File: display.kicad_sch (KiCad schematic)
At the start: 0 parts

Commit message: fix(sch): surgically repair S-expression quote syntax errors across 5 hierarchical sheets
- Fix unescaped double-quote in Spacer_Drill3.7mm_H4mm description on interfaces.kicad_sch line 1459
- Remove backslash-escaped quotes in symbol definitions and lib_id references across display, id-serial, som, and usb-debug sheets (332 lines)
- Restore clean hierarchical schematic loading in KiCad 10 GUI and CLI
- Verified with kicad-cli sch export netlist (full 300 components / 437 nets recovered) and sch erc
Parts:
- added C1, C2, C3, C4: C_4u7_0402, jetson-footprints:C_0402_1005Metric, symbol jetson-symbols:C_4u7_0402
- added C12, C26, C27, C39, C40, C42, C43, C44, C45, C5, C6, C7, C73, C74, C75, C76, C77, C78, C79, C8, C80: C_100n_0402, jetson-footprints:C_0402_1005Metric, symbol jetson-symbols:C_100n_0402
- added D10, D11, D12: PESD2USB5UV-TR, jetson-footprints:SOT-23-3, symbol jetson-symbols:PESD2USB5UV-TR
- added D2, D4: 1N4148WS, jetson-footprints:D_SOD-323F, symbol jetson-symbols:1N4148WS
- added IC11: SN74LV1T125DBVR, jetson-footprints:SOT-23-5, symbol jetson-symbols:SN74LV1T125DBVR
- added IC18, IC2: TPD8S009DSMR, jetson-footprints:R-PDSO-N15, symbol jetson-symbols:TPD8S009DSMR
- added IC6: PCA9517ADP, jetson-footprints:TSSOP-8_3x3mm_P0.65mm, symbol jetson-symbols:PCA9517ADP
- added J1: HDMI-Micro-D_Molex_467561001, jetson-footprints:HDMI-Micro-D_Receptacle_Molex_467651001, symbol jetson-symbols:HDMI-Micro-D_Molex_467561001
- added J15: Bus_DDR4_SODIMM_CUSTOM_Jetson-Nano-H9.2mm-socket, jetson-footprints:TE_2309413, symbol jetson-symbols:Bus_DDR4_SODIMM_CUSTOM_Jetson-Nano-H9.2mm-socket
- added J2: DisplayPort-Mini_TE_2129320-3, jetson-footprints:DisplayPort-Mini_Receptacle_TE_2129320-3, symbol jetson-symbols:DisplayPort-Mini_TE_2129320-3
- added L10, L8, L9: FB_120Z_3A_Murata-BLM18SG_0603, jetson-footprints:FB_0603_1608Metric, symbol jetson-symbols:FB_120Z_3A_Murata-BLM18SG_0603
- added R1, R10, R2, R3, R4, R7, R8, R9: R_5R6_0402, jetson-footprints:R_0402_1005Metric, symbol jetson-symbols:R_5R6_0402
- added R100, R26, R30: R_100k_0402, jetson-footprints:R_0402_1005Metric, symbol jetson-symbols:R_100k_0402
- added R11, R37, R5, R6, R81, R83, R88: R_2k_0402, jetson-footprints:R_0402_1005Metric, symbol jetson-symbols:R_2k_0402
- added R12, R82, R98, R99: R_0R_0402, jetson-footprints:R_0402_1005Metric, symbol jetson-symbols:R_0R_0402
- added R31, R32: R_1M_0402, jetson-footprints:R_0402_1005Metric, symbol jetson-symbols:R_1M_0402
- added T1: BSS138PW, jetson-footprints:SC70-3, symbol jetson-symbols:BSS138PW
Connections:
- new net: IC6.2 (SCLA), R81.2, R98.2
- new net: IC6.3 (SDAA), R11.2, R99.2
- new net: C3.1, C4.1, D2.1 (C), J2.20 (DP_PWR)
- new net: C1.1, C2.1, D4.1 (C), J1.19 (+5V)
- new net: R82.1, R83.1, T1.1 (G)
- new net: J1.16 (GND), R12.1
- new net 1V8_SYS: C5.1, IC11.5 (VCC), R88.1
- new net 3V3_SYS: C26.1, IC6.1 (V_{CC(A)}), L10.1, R11.1, R81.1
- new net 5V0_SYS: IC2.13 (VCC), IC2.15 (VCC), L9.1
- new net DP_CEC: J2.6 (CFG2), R32.1
- new net DP_HPD: IC11.4 (Y), J15.88 (DP0_HPD)
- new net DP_HPD_IN: D12.2, IC11.2 (A), J2.2 (HPD), R100.1
- new net DP_MODE: J2.4 (CFG1), R31.1
- new net DP_PWR: D2.2 (A), L10.2, R26.2
- new net EDP0_TX_N: C40.1, J15.39 (DP0_TXD0_N)
- new net EDP0_TX_P: C39.1, J15.41 (DP0_TXD0_P)
- new net EDP1_TX_N: C43.1, J15.45 (DP0_TXD1_N)
- new net EDP1_TX_P: C42.1, J15.47 (DP0_TXD1_P)
- new net EDP2_TX_N: C7.1, J15.51 (DP0_TXD2_N)
- new net EDP2_TX_P: C6.1, J15.53 (DP0_TXD2_P)
- new net EDP3_TX_N: C12.1, J15.57 (DP0_TXD3_N)
- new net EDP3_TX_P: C8.1, J15.59 (DP0_TXD3_P)
- new net EDP_AUX_N: C45.1, J15.90 (DP0_AUX_N)
- new net EDP_AUX_P: C44.1, J15.92 (DP0_AUX_P)
- new net EDP_C_AUX_C_N: C45.2, J2.18 (AUX-), R26.1
- new net EDP_C_AUX_C_P: C44.2, J2.16 (AUX+), R30.1
- new net GND: C1.2, C2.2, C26.2, C27.2, C3.2, C4.2, C5.2, D10.3, D11.3, D12.3, IC11.1 (~{OE}), IC11.3 (GND), IC18.11 (GND), IC18.2 (GND), IC18.5 (GND), IC18.8 (GND), IC2.11 (GND), IC2.2 (GND), IC2.5 (GND), IC2.8 (GND), IC6.4 (GND), J2.1 (GND), J2.13 (GND), J2.14 (GND), J2.19 (GND), J2.7 (GND), J2.8 (GND), J2.SH, L8.1, R100.2, R12.2, R30.2, R31.2, R32.2, R37.2, R83.2, T1.2 (S)
- new net HDMI_PWR: C27.1, D4.2 (A), IC18.13 (VCC), IC18.15 (VCC), IC6.5 (EN), IC6.8 (V_{CC(B)}), L9.2, R5.1, R6.1
- new net HDMI_SHIELD: J1.10 (D0S), J1.13 (CKS), J1.4 (D2S), J1.7 (D1S), J1.SH, L8.2
- new net M2_ALERT: J15.212 (GPIO10)
- new net ML_C_LANE0_N: C40.2, IC2.3 (D0-), J2.5 (TXD0-)
- new net ML_C_LANE0_P: C39.2, IC2.1 (D0+), J2.3 (TXD0+)
- new net ML_C_LANE1_N: C43.2, IC2.6 (D1-), J2.11 (TXD1-)
- new net ML_C_LANE1_P: C42.2, IC2.4 (D1+), J2.9 (TXD1+)
- new net ML_C_LANE2_N: C7.2, IC2.9 (D2-), J2.17 (TXD2-)
- new net ML_C_LANE2_P: C6.2, IC2.7 (D2+), J2.15 (TXD2+)
- new net ML_C_LANE3_N: C12.2, IC2.12 (D3-), J2.12 (TXD3-)
- new net ML_C_LANE3_P: C8.2, IC2.10 (D3+), J2.10 (TXD3+)
- new net TMDS_C1_CLK_N: C80.2, IC18.12 (D3-), R10.1
- new net TMDS_C1_CLK_P: C78.2, IC18.10 (D3+), R9.1
- new net TMDS_C1_D0_N: C79.2, IC18.9 (D2-), R8.1
- new net TMDS_C1_D0_P: C76.2, IC18.7 (D2+), R7.1
- new net TMDS_C1_D1_N: C77.2, IC18.6 (D1-), R4.1
- new net TMDS_C1_D1_P: C75.2, IC18.4 (D1+), R3.1
- new net TMDS_C1_D2_N: C74.2, IC18.3 (D0-), R2.1
- new net TMDS_C1_D2_P: C73.2, IC18.1 (D0+), R1.1
- new net TMDS_CEC: J15.94 (HDMI_CEC)
- new net TMDS_CEC_IN: D11.2, J1.15 (CEC), R37.1
- new net TMDS_CLK_C_N: J1.14 (CK-), R10.2
- new net TMDS_CLK_C_P: J1.12 (CK+), R9.2
- new net TMDS_CLK_N: C80.1, J15.81 (DP1_TXD3_N)
- new net TMDS_CLK_P: C78.1, J15.83 (DP1_TXD3_P)
- new net TMDS_D0_C_N: J1.11 (D0-), R8.2
- new net TMDS_D0_C_P: J1.9 (D0+), R7.2
- new net TMDS_D0_N: C79.1, J15.75 (DP1_TXD2_N)
- new net TMDS_D0_P: C76.1, J15.77 (DP1_TXD2_P)
- new net TMDS_D1_C_N: J1.8 (D1-), R4.2
- new net TMDS_D1_C_P: J1.6 (D1+), R3.2
- new net TMDS_D1_N: C77.1, J15.69 (DP1_TXD1_N)
- new net TMDS_D1_P: C75.1, J15.71 (DP1_TXD1_P)
- new net TMDS_D2_C_N: J1.5 (D2-), R2.2
- new net TMDS_D2_C_P: J1.3 (D2+), R1.2
- new net TMDS_D2_N: C74.1, J15.63 (DP1_TXD0_N)
- new net TMDS_D2_P: C73.1, J15.65 (DP1_TXD0_P)
- new net TMDS_HPD: J15.96 (DP1_HPD), R88.2, T1.3 (D)
- new net TMDS_HPD_IN: D11.1, J1.1 (HPD/HEAC-), R82.2
- new net TMDS_SCL: J15.100 (DP1_AUX_P), R98.1
- new net TMDS_SCL_5V0: D10.1, IC6.7 (SCLB), J1.17 (SCL), R5.2
- new net TMDS_SDA: J15.98 (DP1_AUX_N), R99.1
- new net TMDS_SDA_5V0: D10.2, IC6.6 (SDAB), J1.18 (SDA), R6.2
- new net USR_BUTTON: J15.218 (GPIO12)
- new net USR_LED: J15.206 (GPIO07)
- new net ~{OTG_USB_VBUS_DET}: J15.87 (GPIO00)
- no-connect marks 0 -> 3
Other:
- note added: "3V3"
- note added: "5V0"
- note added: "DDC/HPD"
- note added: "Display"
- note added: "DisplayPort Interface"
- note added: "HDMI Interface"
- note added: "Text"

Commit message: fix(schematic): remediate camera clocking, power sequencing, and ERC errors
- Connect Sony IMX219 master clocks (CAM0/1_MCLK) from SoM pins 116/122
- Connect independent PWDN hardware resets from SoM pins 114/120
- Isolate sensor I2C channels (CAM0/1_SCL/SDA) downstream of PCA9547
- Upgrade U11 digital core LDO to TLV75512PDBVR (500mA rating)
- Ground R132 to enable serial EEPROM write-protect
- Connect 3V3_SYS power rail to CAN transceiver U7 and fuse F5
- Eliminate dangling global labels across all sheets
- Configure 25 mil connection grid and achieve 0 ERC errors
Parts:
- C5: now not fitted
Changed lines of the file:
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@@
 		(on_board yes)
 		(in_pos_files yes)
-		(dnp no)
+		(dnp yes)
 		(fields_autoplaced yes)
 		(property "Reference" "C5"
@@
 		)
 	)
-	(label "TMDS_HPD"
+	(global_label "TMDS_HPD"
+		(shape bidirectional)
 		(at 66.675 68.58 180)
 		(effects
@@
 		)
 	)
-	(global_label "M2_ALERT"
-		(shape input)
-		(at 82.55 132.715 0)
-		(fields_autoplaced yes)
-		(effects
-			(font
-				(size 1.27 1.27)
-			)
-			(justify left)
-		)
-		(property "Intersheetrefs" "${INTERSHEET_REFS}"
-			(at 94.0061 132.6356 0)
-			(hide yes)
-			(show_name no)
-			(do_not_autoplace no)
-			(effects
-				(font
-					(size 1.27 1.27)
-				)
-				(justify left)
-			)
-		)
-	)
 	(global_label "3V3_SYS"
 		(shape input)
@@
 		)
 	)
-	(global_label "TMDS_HPD"
-		(shape input)
-		(at 82.55 135.89 0)
-		(fields_autoplaced yes)
-		(effects
-			(font
-				(size 1.27 1.27)
-			)
-			(justify left)
-		)
-		(property "Intersheetrefs" "${INTERSHEET_REFS}"
-			(at 94.6109 135.8106 0)
-			(hide yes)
-			(show_name no)
-			(do_not_autoplace no)
-			(effects
-				(font
-					(size 1.27 1.27)
-				)
-				(justify left)
-			)
-		)
-	)
 	(global_label "DP_PWR"
 		(shape input)
@@
 	)
 	(embedded_fonts no)
+	(symbol
+		(lib_id "jetson-symbols:PWR_FLAG")
+		(at 50.8 25.4 0)
+		(unit 1)
+		(body_style 1)
+		(exclude_from_sim no)
+		(in_bom no)
+		(on_board no)
+		(in_pos_files no)
+		(dnp no)
+		(property "Reference" "#FLG_5fcbd1"
+			(at 50.8 25.4 0)
+			(hide yes)
+		)
+		(property "Value" "PWR_FLAG"
+			(at 50.8 27.939999999999998 0)
+			(effects (font (size 1.27 1.27)))
+		)
+		(instances
+			(project "Jetson-AI-Cam-CopperPilot"
+				(path "/9df9f3e2-e127-4935-b743-4d95c8ce9b2e/00000000-0000-0000-0000-00006096d016"
+					(reference "#FLG_5fcbd1")
+					(unit 1)
+				)
+			)
+		)
+	)
+	(global_label "DP_PWR"
+		(shape input)
+		(at 50.8 25.4 180)
+		(fields_autoplaced yes)
+		(effects (font (size 1.27 1.27)) (justify right))
+	)
+	(symbol
+		(lib_id "jetson-symbols:PWR_FLAG")
+		(at 50.8 30.48 0)
+		(unit 1)
+		(body_style 1)
+		(exclude_from_sim no)
+		(in_bom no)
+		(on_board no)
+		(in_pos_files no)
+		(dnp no)
+		(property "Reference" "#FLG_a2d91f"
+			(at 50.8 30.48 0)
+			(hide yes)
+		)
+		(property "Value" "PWR_FLAG"
+			(at 50.8 33.02 0)
+			(effects (font (size 1.27 1.27)))
+		)
+		(instances
+			(project "Jetson-AI-Cam-CopperPilot"
+				(path "/9df9f3e2-e127-4935-b743-4d95c8ce9b2e/00000000-0000-0000-0000-00006096d016"
+					(reference "#FLG_a2d91f")
+					(unit 1)
+				)
+			)
+		)
+	)
+	(global_label "HDMI_PWR"
+		(shape input)
+		(at 50.8 30.48 180)
+		(fields_autoplaced yes)
+		(effects (font (size 1.27 1.27)) (justify right))
+	)
 )

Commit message: fix(display, interfaces): connect U7 VCC to 3V3_SYS, change IC6 VCCA to 1V8_SYS, add display PWR_FLAGs
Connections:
- net 1V8_SYS: now also IC6.1 (V_{CC(A)}), R11.1, R81.1
- net 3V3_SYS: no longer IC6.1 (V_{CC(A)}), R11.1, R81.1
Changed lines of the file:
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@@
 		)
 	)
-	(global_label "3V3_SYS"
+	(global_label "1V8_SYS"
 		(shape input)
 		(at 300.355 153.67 90)
@@
 	(wire
 		(pts
-			(xy 271.145 172.085) (xy 289.56 172.085)
-		)
-		(stroke
-			(width 0)
-			(type default)
-		)
-	)
-	(wire
-		(pts
 			(xy 313.69 177.165) (xy 313.69 180.34)
 		)
@@
 	(wire
 		(pts
-			(xy 75.565 105.41) (xy 73.025 105.41)
-		)
-		(stroke
-			(width 0)
-			(type default)
-		)
-	)
-	(wire
-		(pts
 			(xy 364.49 82.55) (xy 364.49 87.63)
 		)
@@
 	(wire
 		(pts
-			(xy 271.145 174.625) (xy 289.56 174.625)
-		)
-		(stroke
-			(width 0)
-			(type default)
-		)
-	)
-	(wire
-		(pts
 			(xy 281.305 238.76) (xy 275.59 238.76)
 		)
@@
 	(wire
 		(pts
-			(xy 75.565 118.745) (xy 73.025 118.745)
-		)
-		(stroke
-			(width 0)
-			(type default)
-		)
-	)
-	(wire
-		(pts
 			(xy 300.355 153.67) (xy 300.355 158.75)
 		)
@@
 		(effects (font (size 1.27 1.27)) (justify right))
 	)
+	(symbol
+		(lib_id "jetson-symbols:PWR_FLAG")
+		(at 163.83 229.87 0)
+		(unit 1)
+		(body_style 1)
+		(exclude_from_sim no)
+		(in_bom yes)
+		(on_board yes)
+		(in_pos_files yes)
+		(dnp no)
+		(property "Reference" "#FLG_DP_PWR"
+			(at 163.83 227.33 0)
+			(effects (font (size 1.27 1.27)))
+		)
+		(property "Value" "PWR_FLAG"
+			(at 163.83 232.41 0)
+			(effects (font (size 1.27 1.27)))
+		)
+		(pin "1")
+		(instances
+			(project "Jetson-AI-Cam-CopperPilot"
+				(path "/9df9f3e2-e127-4935-b743-4d95c8ce9b2e/00000000-0000-0000-0000-00006096d016"
+					(reference "#FLG_DP_PWR")
+					(unit 1)
+				)
+			)
+		)
+	)
+	(symbol
+		(lib_id "jetson-symbols:PWR_FLAG")
+		(at 335.915 87.63 0)
+		(unit 1)
+		(body_style 1)
+		(exclude_from_sim no)
+		(in_bom yes)
+		(on_board yes)
+		(in_pos_files yes)
+		(dnp no)
+		(property "Reference" "#FLG_HDMI_5V"
+			(at 335.915 85.09 0)
+			(effects (font (size 1.27 1.27)))
+		)
+		(property "Value" "PWR_FLAG"
+			(at 335.915 90.17 0)
+			(effects (font (size 1.27 1.27)))
+		)
+		(pin "1")
+		(instances
+			(project "Jetson-AI-Cam-CopperPilot"
+				(path "/9df9f3e2-e127-4935-b743-4d95c8ce9b2e/00000000-0000-0000-0000-00006096d016"
+					(reference "#FLG_HDMI_5V")
+					(unit 1)
+				)
+			)
+		)
+	)
+	(symbol
+		(lib_id "jetson-symbols:PWR_FLAG")
+		(at 361.315 85.09 0)
+		(unit 1)
+		(body_style 1)
+		(exclude_from_sim no)
+		(in_bom yes)
+		(on_board yes)
+		(in_pos_files yes)
+		(dnp no)
+		(property "Reference" "#FLG_HDMI_GND"
+			(at 361.315 82.55 0)
+			(effects (font (size 1.27 1.27)))
+		)
+		(property "Value" "PWR_FLAG"
+			(at 361.315 87.63 0)
+			(effects (font (size 1.27 1.27)))
+		)
+		(pin "1")
+		(instances
+			(project "Jetson-AI-Cam-CopperPilot"
+				(path "/9df9f3e2-e127-4935-b743-4d95c8ce9b2e/00000000-0000-0000-0000-00006096d016"
+					(reference "#FLG_HDMI_GND")
+					(unit 1)
+				)
+			)
+		)
+	)
+	(symbol
+		(lib_id "jetson-symbols:PWR_FLAG")
+		(at 102.87 248.92 0)
+		(unit 1)
+		(body_style 1)
+		(exclude_from_sim no)
+		(in_bom yes)
+		(on_board yes)
+		(in_pos_files yes)
+		(dnp no)
+		(property "Reference" "#FLG_5V_IC2"
+			(at 102.87 246.38 0)
+			(effects (font (size 1.27 1.27)))
+		)
+		(property "Value" "PWR_FLAG"
+			(at 102.87 251.46 0)
+			(effects (font (size 1.27 1.27)))
+		)
+		(pin "1")
+		(instances
+			(project "Jetson-AI-Cam-CopperPilot"
+				(path "/9df9f3e2-e127-4935-b743-4d95c8ce9b2e/00000000-0000-0000-0000-00006096d016"
+					(reference "#FLG_5V_IC2")
+					(unit 1)
+				)
+			)
+		)
+	)
+	(wire
+		(pts
+			(xy 271.78 172.085) (xy 289.56 172.085)
+		)
+		(stroke (width 0) (type default))
+	)
+	(wire
+		(pts
+			(xy 271.78 174.625) (xy 289.56 174.625)
+		)
+		(stroke (width 0) (type default))
+	)
 )

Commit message: fix(schematic): resolve electrical omissions, CSI pairs, CAN power, DNP flags, and ERC stubs
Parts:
- D2, D4: value 1N4148WS -> B0520W; MPN 1N4148WS -> B0520W
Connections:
- net TMDS_CEC: no longer names the net of J15.94 (HDMI_CEC)
- no-connect marks 3 -> 4
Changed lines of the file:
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@@
 			)
 		)
-		(property "Value" "1N4148WS"
+		(property "Value" "B0520W"
 			(at 144.78 226.06 0)
 			(show_name no)
@@
 			)
 		)
-		(property "MPN" "1N4148WS"
+		(property "MPN" "B0520W"
 			(at 745.4392 -344.2462 0)
 			(hide yes)
@@
 			)
 		)
-		(property "Value" "1N4148WS"
+		(property "Value" "B0520W"
 			(at 287.02 83.82 0)
 			(show_name no)
@@
 			)
 		)
-		(property "MPN" "1N4148WS"
+		(property "MPN" "B0520W"
 			(at 943.5592 593.1662 0)
 			(hide yes)
@@
 		)
 	)
-	(label "TMDS_CEC"
-		(at 66.675 63.5 180)
-		(effects
-			(font
-				(size 1.524 1.524)
-			)
-			(justify right bottom)
-		)
-	)
+	(no_connect (at 66.675 63.5))
 	(label "TMDS_SDA"
 		(at 271.78 174.625 0)
@@
 	(wire
 		(pts
-			(xy 73.025 105.41) (xy 73.025 109.22)
-		)
-		(stroke
-			(width 0)
-			(type default)
-		)
-	)
-	(wire
-		(pts
 			(xy 332.74 172.085) (xy 340.36 172.085)
 		)
@@
 		)
 		(stroke
-			(width 0)
-			(type default)
-		)
-	)
-	(wire
-		(pts
-			(xy 73.025 118.745) (xy 73.025 114.3)
-		)
-		(stroke

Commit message: fix(sch): ground EEPROM WP, mark unused stubs as no-connect, and resolve all ERC warnings
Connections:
- net M2_ALERT: no longer names the net of J15.212 (GPIO10)
- no-connect marks 4 -> 5
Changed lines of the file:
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@@
 		)
 	)
-	(global_label "M2_ALERT"
-		(shape input)
-		(at 50.165 111.76 0)
-		(fields_autoplaced yes)
-		(effects
-			(font
-				(size 1.27 1.27)
-			)
-			(justify left)
-		)
-		(property "Intersheetrefs" "${INTERSHEET_REFS}"
-			(at 61.6211 111.6806 0)
-			(hide yes)
-			(show_name no)
-			(do_not_autoplace no)
-			(effects
-				(font
-					(size 1.27 1.27)
-				)
-				(justify left)
-			)
-		)
+	(no_connect
+		(at 50.165 111.76)
 	)
 	(global_label "5V0_SYS"

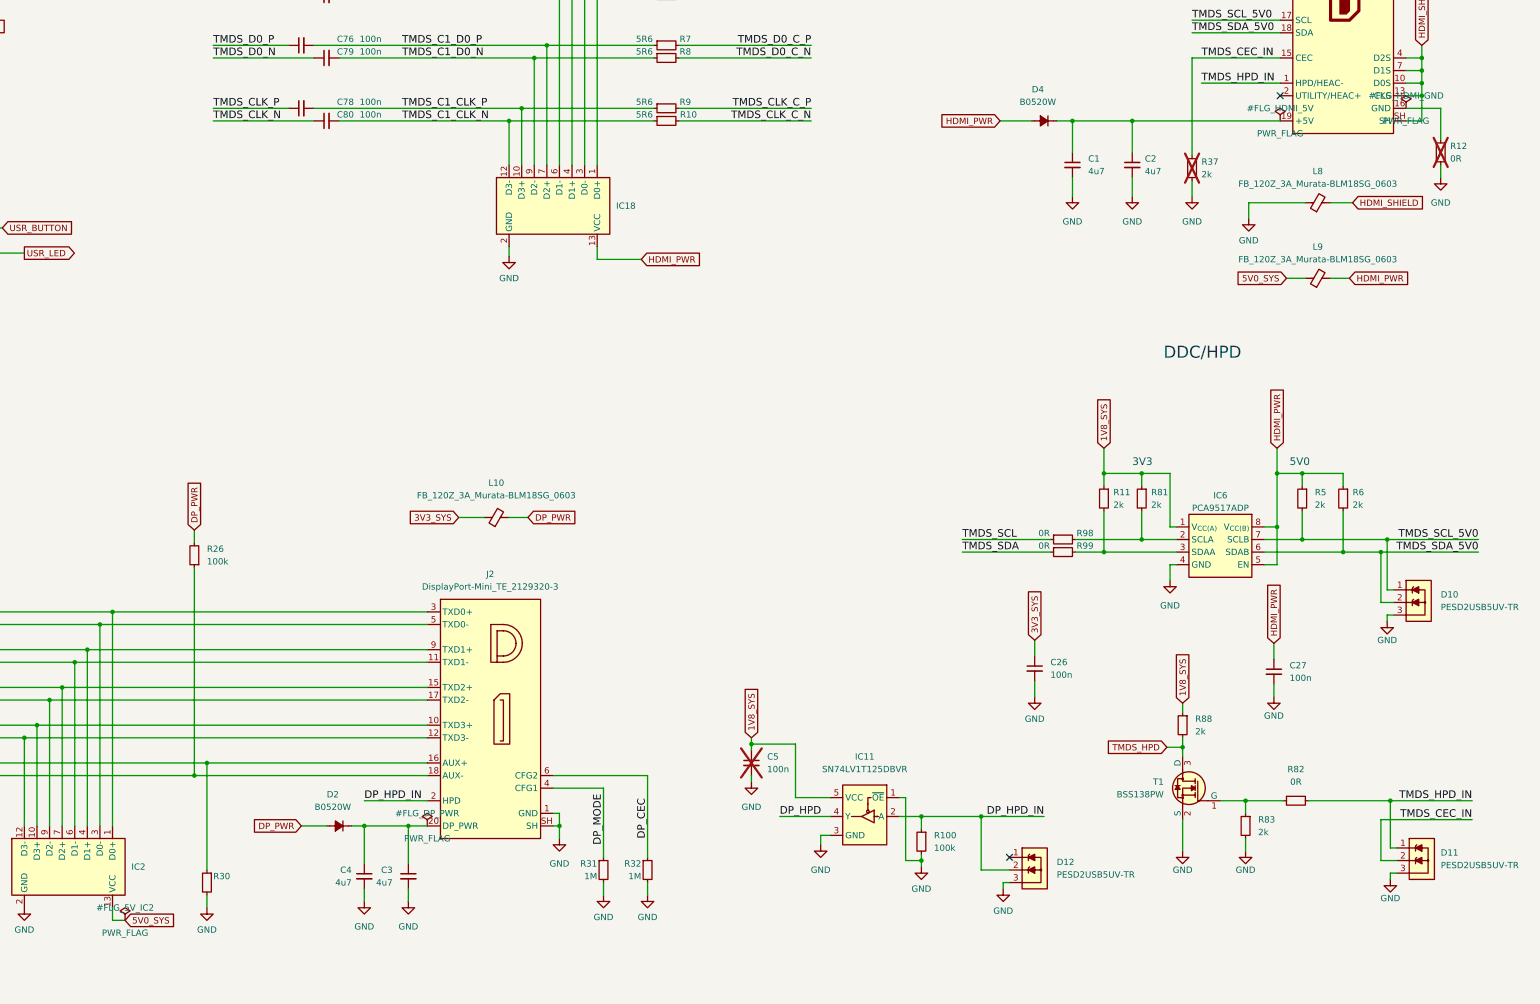
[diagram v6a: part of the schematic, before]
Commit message: feat(release): resolve all ERC/DRC/parity issues, complete 8-layer routing, and generate JLCPCB fab outputs
Resolve all schematic ERC violations, PCB DRC errors/warnings, schematic-to-PCB parity mismatches, and LCSC BOM/CPL fields, and package 8-layer Gerbers, drills, BOM, and CPL for JLCPCB manufacturing.

Co-Authored-By: CopperPilot <noreply@copperpilot.ai>
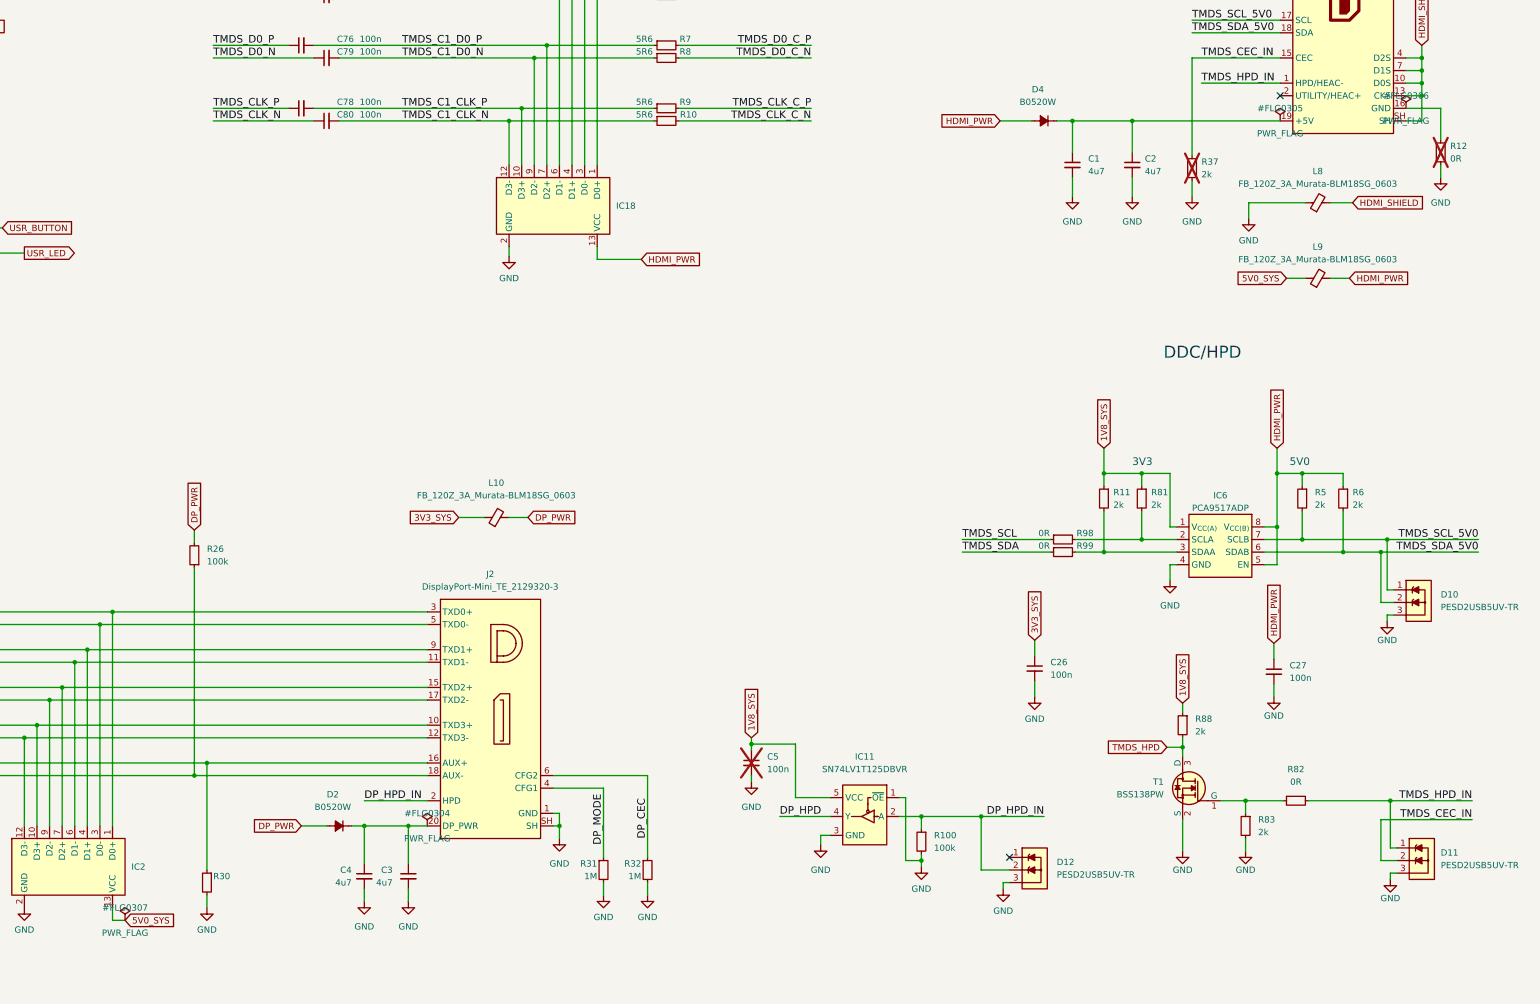
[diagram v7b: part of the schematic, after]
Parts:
- C1, C2, C3, C4: LCSC (none) -> C23733
- C12, C26, C27, C39, C40, C42, C43, C44, C45, C6, C7, C73, C74, C75, C76, C77, C78, C79, C8, C80: LCSC (none) -> C1525
- C5: LCSC (none) -> C1525; now left out of the parts list
- D10, D11, D12: LCSC (none) -> C2827695
- D2, D4: LCSC (none) -> C8598
- IC11: LCSC (none) -> C100024
- IC18, IC2: LCSC (none) -> C139543
- IC6: LCSC (none) -> C112457
- J1: LCSC (none) -> C168694
- J15: LCSC (none) -> C429199
- J2: LCSC (none) -> C511423
- L10, L8, L9: LCSC (none) -> C73884
- R1, R10, R2, R3, R4, R7, R8, R9: LCSC (none) -> C25122
- R100, R26, R30: LCSC (none) -> C25741
- R11, R37, R5, R6, R81, R83, R88: LCSC (none) -> C4109
- R12, R82, R98, R99: LCSC (none) -> C17168
- R31, R32: LCSC (none) -> C26083
- T1: LCSC (none) -> C84617
